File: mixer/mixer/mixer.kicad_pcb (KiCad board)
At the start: 2 copper layers, 80 x 100 mm, 41 parts, among them J1 Power Connector, J10 Output, J11 Inverted, J2 Input 1, J3 Input 2, J4 Input 3, J5 Input 4, J6 Front_Board_Con, J7 Front_Board_Balance, J8 Back_Board_Conn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

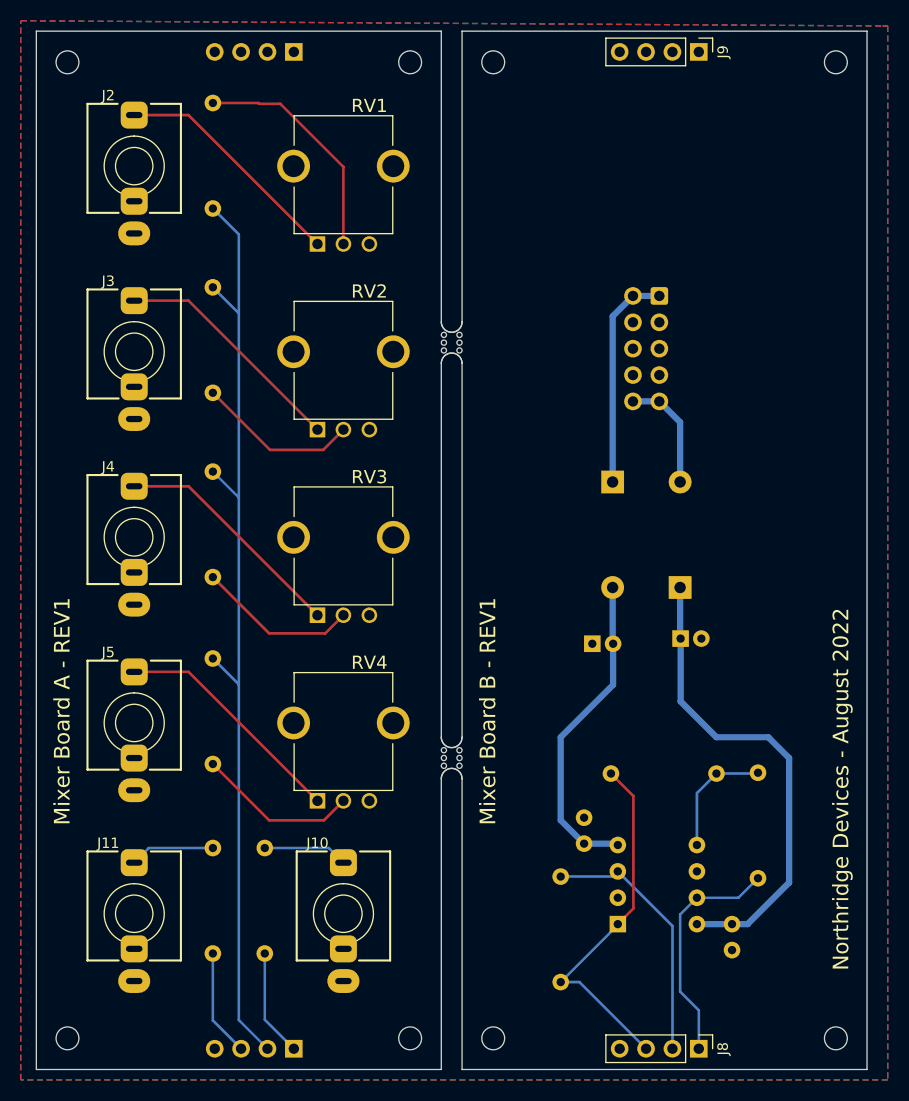
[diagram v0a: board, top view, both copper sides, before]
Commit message: Updated mixer and multiple to use new common libs
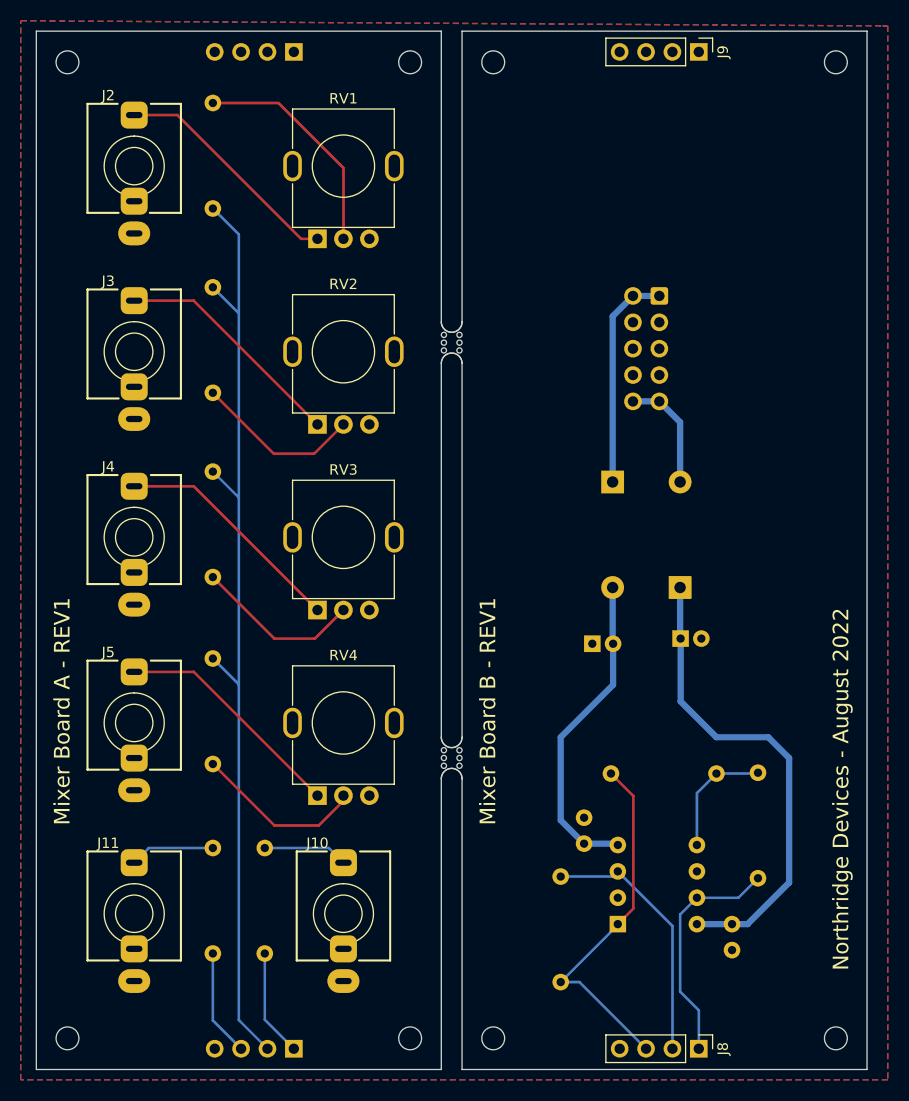
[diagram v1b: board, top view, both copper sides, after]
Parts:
- RV1, RV2, RV3, RV4: footprint SamacSys_Parts:RD901F4015R1B100K00DL1 -> Alpha_Pots:Potentiometer_Alpha_RV09AF-40-20K_Single_Vertical
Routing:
- net Net-(R3-Pad1): track 15.5 -> 16.2 mm
- net Net-(R1-Pad2): track 22.5 -> 22.0 mm
- net Net-(R2-Pad1): track 15.7 -> 16.2 mm

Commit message: Partially converted keyboard libaries over to common dir
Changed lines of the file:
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@@
     (fp_line (start 5.72 -15.26) (end -3.18 -15.26) (layer "B.Fab") (width 0.1))
     (fp_line (start -3.18 -15.26) (end -3.18 4.1) (layer "B.Fab") (width 0.1))
-    (pad "1" thru_hole roundrect (at 0 0 180) (size 1.7 1.7) (drill 1) (layers *.Cu *.Mask) (roundrect_rratio 0.147059)
+    (pad "1" thru_hole roundrect (at 0 0 180) (size 1.7 1.7) (drill 1) (layers *.Cu *.Mask) (roundrect_rratio 0.1470588235)
       (net 5 "Net-(D2-Pad1)") (pinfunction "Pin_1") (pintype "passive"))
     (pad "2" thru_hole circle (at 2.54 0 180) (size 1.7 1.7) (drill 1) (layers *.Cu *.Mask)

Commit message: Added rev2 of mixer. Fixed opamp configuation and panel connector layout
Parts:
- moved J1 10.5 mm to (147.4, 55.7), turned to 0 degrees
- moved J8 2.00 mm to (155.8, 118.0)
- moved J9 2.00 mm to (155.8, 22.0)
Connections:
- RV1 pad 1: Net-(J2-PadT) -> GND
- RV1 pad 3: GND -> Net-(J2-PadT)
- RV2 pad 1: Net-(J3-PadT) -> GND
- RV2 pad 3: GND -> Net-(J3-PadT)
- RV3 pad 1: Net-(J4-PadT) -> GND
- RV3 pad 3: GND -> Net-(J4-PadT)
- RV4 pad 1: Net-(J5-PadT) -> GND
- RV4 pad 3: GND -> Net-(J5-PadT)
- U1 pad 2: GND -> INPUT_MIX_BACK
- U1 pad 3: INPUT_MIX_BACK -> GND
- U1 pad 5: Net-(R6-Pad1) -> GND
- U1 pad 6: GND -> Net-(R6-Pad1)
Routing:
- net Net-(D1-Pad2): track 11.1 -> 21.3 mm
- net Net-(D2-Pad1): track 21.3 -> 11.3 mm
- net Net-(J4-PadT): track 22.6 -> 27.6 mm
- net Net-(J5-PadT): track 22.6 -> 27.6 mm
- net Net-(J2-PadT): track 22.6 -> 27.6 mm
- net Net-(J3-PadT): track 22.6 -> 27.5 mm
- net OUTPUT_INV_BACK: track 34.7 -> 38.7 mm
- net Net-(R6-Pad1): track 11.6 -> 14.1 mm
- net INPUT_MIX_BACK: track 25.0 -> 23.6 mm
- net OUTPUT_BACK: track 22.6 -> 23.6 mm
- net Net-(R2-Pad1): track 16.2 -> 15.6 mm
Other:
- board text added: "Mixer Board A - REV2"
- board text added: "Mixer Board B - REV2"
- board text removed: "Mixer Board A - REV1"
- board text removed: "Mixer Board B - REV1"
